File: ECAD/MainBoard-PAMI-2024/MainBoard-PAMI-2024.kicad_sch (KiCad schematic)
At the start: 41 parts, among them J1 Selecteur-Robot, J10 Serial, J2 USB_B, J3 Tirette, J4 Servo, J5 Sensor_Right, J6 Sensor_Left, J7 Conn_01x04, J8 Conn_01x04, J9 Tirette, SW1 SW_Push, SW2 SW_Push, U1 ESP32-S3-WROOM-1, U2 AMS1117-3.3, U3 Photointerrupteur

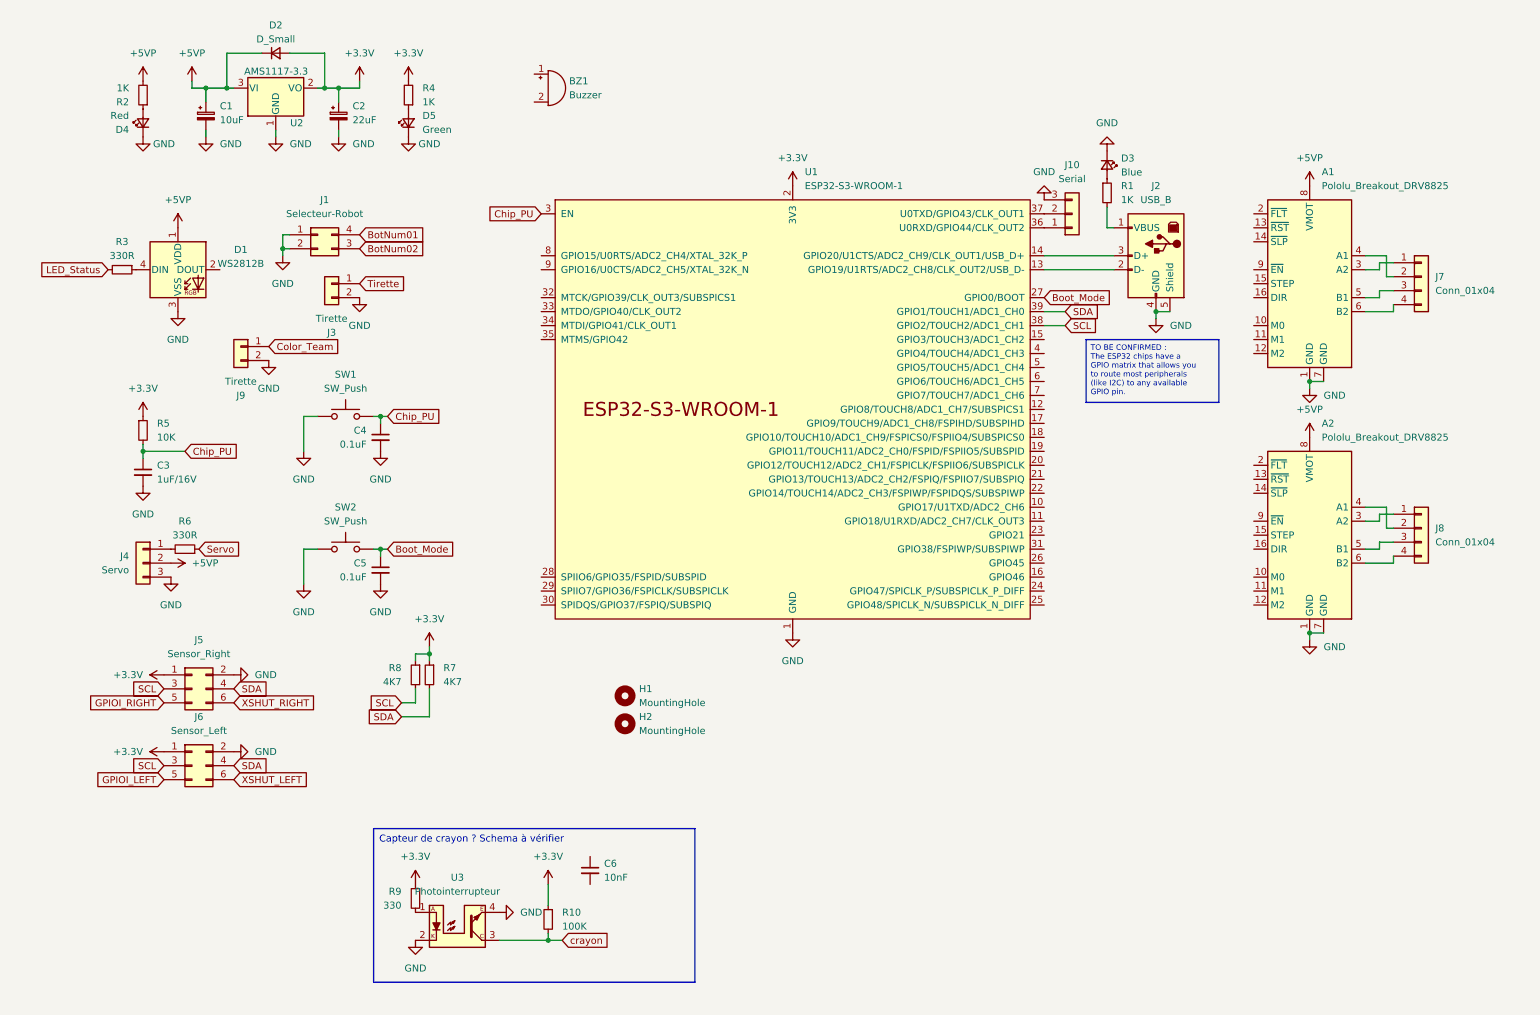
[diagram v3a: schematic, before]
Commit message: add TMC2208 reorgnise components
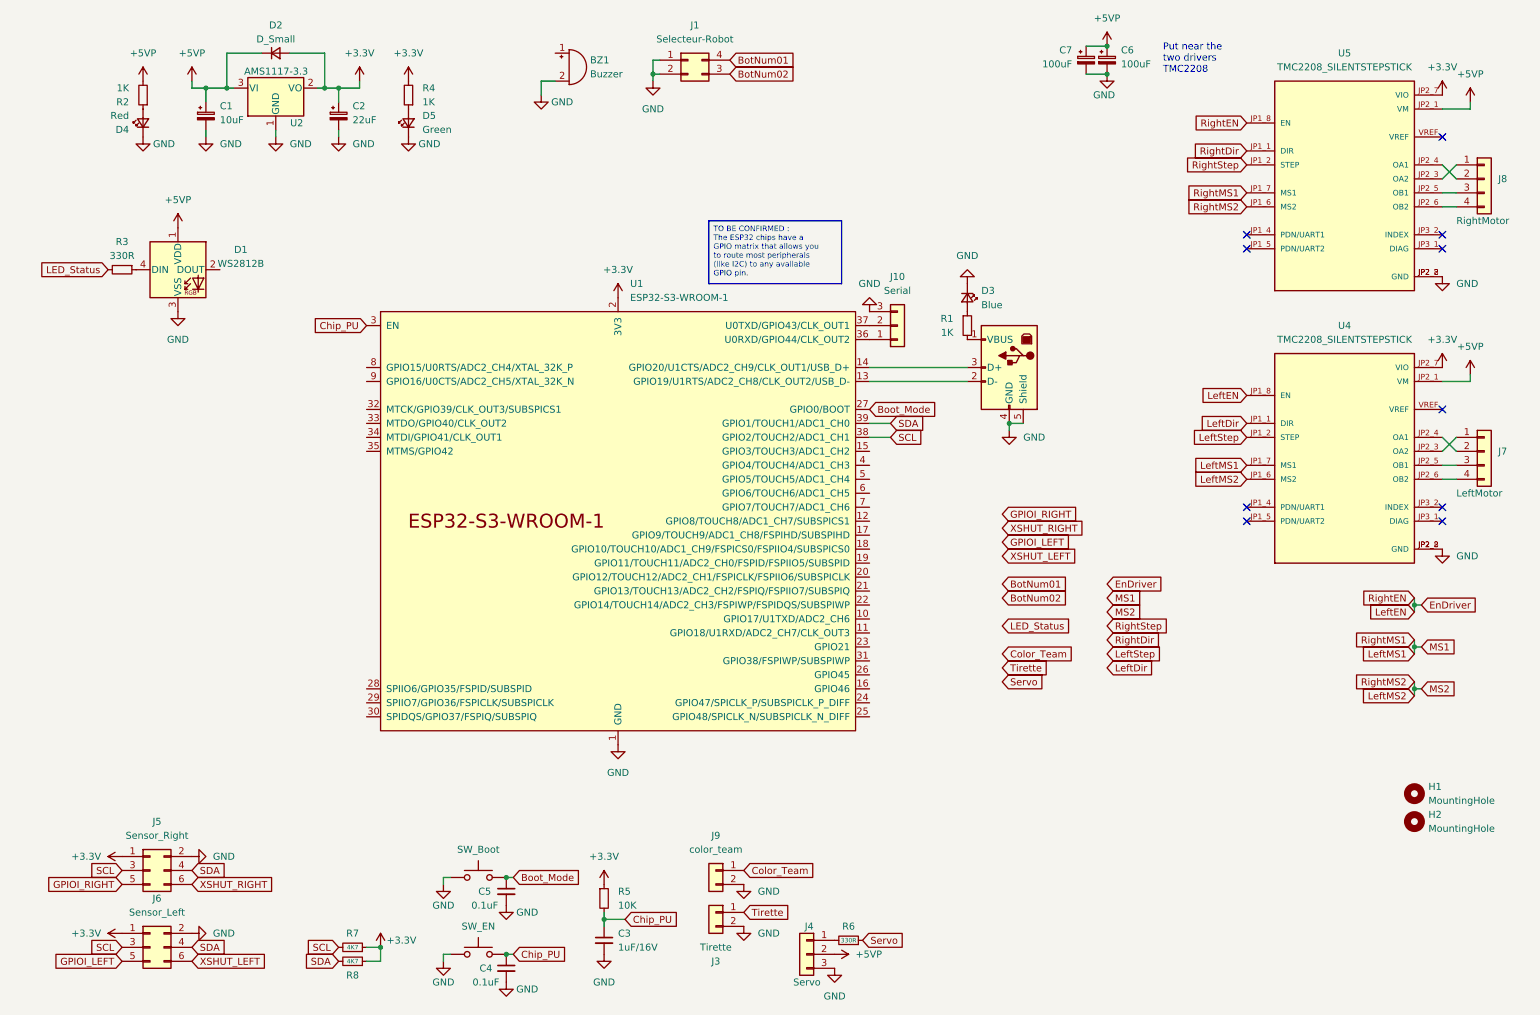
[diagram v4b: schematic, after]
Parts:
- removed A1, A2: Pololu_Breakout_DRV8825, Module:Pololu_Breakout-16_15.2x20.3mm, symbol Driver_Motor:Pololu_Breakout_DRV8825
- removed C6: 10nF, symbol Device:C_Small
- removed R10: 100K, Resistor_SMD:R_1206_3216Metric_Pad1.30x1.75mm_HandSolder, symbol Device:R_Small
- removed R9: 330, Resistor_SMD:R_1206_3216Metric_Pad1.30x1.75mm_HandSolder, symbol Device:R_Small
- removed U3: Photointerrupteur, symbol Sensor_Proximity:ITR9608-F
- added C6, C7: 100uF, symbol Device:C_Polarized_Small
- added U4, U5: TMC2208_SILENTSTEPSTICK, TMC2208_SILENTSTEPSTICK:MODULE_TMC2208_SILENTSTEPSTICK, symbol TMC2208_SILENTSTEPSTICK:TMC2208_SILENTSTEPSTICK
- BZ1: footprint (none) -> Buzzer_Beeper:Buzzer_12x9.5RM7.6
- J7: value Conn_01x04 -> LeftMotor
- J8: value Conn_01x04 -> RightMotor
- J9: value Tirette -> color_team
- SW1: value SW_Push -> SW_EN
- SW2: value SW_Push -> SW_Boot
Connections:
- net +3.3V: now also U4.JP2_7 (VIO), U5.JP2_7 (VIO)
- net +5VP: now also C6.1, C7.1, U4.JP2_1 (VM), U5.JP2_1 (VM)
- net GND: now also BZ1.2 (+), C6.2, C7.2, U4.JP2_2 (GND), U4.JP2_8 (GND), U5.JP2_2 (GND), U5.JP2_8 (GND)
- net SCL: now also R7.2; no longer R8.2
- net SDA: now also R8.2; no longer R7.2
- net at J7.1 (Pin_1): now also U4.JP2_3 (OA2)
- net at J7.2 (Pin_2): now also U4.JP2_4 (OA1)
- net at J7.3 (Pin_3): now also U4.JP2_5 (OB1)
- net at J7.4 (Pin_4): now also U4.JP2_6 (OB2)
- net at J8.1 (Pin_1): now also U5.JP2_3 (OA2)
- net at J8.2 (Pin_2): now also U5.JP2_4 (OA1)
- net at J8.3 (Pin_3): now also U5.JP2_5 (OB1)
- net at J8.4 (Pin_4): now also U5.JP2_6 (OB2)
- new net EnDriver: U4.JP1_8 (EN), U5.JP1_8 (EN)
- new net LeftDir: U4.JP1_1 (DIR)
- new net LeftMS1: U4.JP1_7 (MS1), U5.JP1_7 (MS1)
- new net LeftMS2: U4.JP1_6 (MS2), U5.JP1_6 (MS2)
- new net LeftStep: U4.JP1_2 (STEP)
- new net RightDir: U5.JP1_1 (DIR)
- new net RightStep: U5.JP1_2 (STEP)
- no-connect marks 0 -> 10
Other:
- note added: "Put near the two drivers TMC2208"
- moved on the sheet: BZ1, C3, C4, C5, D3, H1, H2, J1, J10, J3, J4, J5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

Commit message: add capacitor for ESP32
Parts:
- added C8: 0.1uF, symbol Device:C_Small
- added C9: 10uF, symbol Device:C_Small
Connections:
- net +3.3V: now also C8.1, C9.1
- net GND: now also C8.2, C9.2
- no-connect marks 10 -> 13
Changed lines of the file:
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@@
   (junction (at 68.58 29.21) (diameter 0) (color 0 0 0 0)
   )
+  (junction (at 111.76 57.15) (diameter 0) (color 0 0 0 0)
+  )
+  (junction (at 111.76 62.23) (diameter 0) (color 0 0 0 0)
+  )
   (junction (at 101.6 172.72) (diameter 0) (color 0 0 0 0)
   )
   (junction (at 193.04 90.17) (diameter 0) (color 0 0 0 0)
+  )
+  (junction (at 121.92 54.61) (diameter 0) (color 0 0 0 0)
   )
   (junction (at 210.82 26.67) (diameter 0) (color 0 0 0 0)
@@
   (no_connect (at 236.22 105.41))
   (no_connect (at 236.22 58.42))
+  (no_connect (at 76.2 140.97))
   (no_connect (at 236.22 55.88))
   (no_connect (at 271.78 105.41))
+  (no_connect (at 76.2 138.43))
   (no_connect (at 271.78 87.63))
   (no_connect (at 236.22 107.95))
   (no_connect (at 271.78 107.95))
+  (no_connect (at 76.2 143.51))
   (no_connect (at 271.78 55.88))
   (no_connect (at 271.78 58.42))
@@
     (stroke (width 0) (type default))
   )
+  (wire (pts (xy 107.95 62.23) (xy 111.76 62.23))
+    (stroke (width 0) (type default))
+  )
   (wire (pts (xy 276.86 31.75) (xy 276.86 33.02))
     (stroke (width 0) (type default))
   )
+  (wire (pts (xy 111.76 57.15) (xy 111.76 54.61))
+    (stroke (width 0) (type default))
+  )
   (wire (pts (xy 193.04 90.17) (xy 195.58 90.17))
     (stroke (width 0) (type default))
@@
     (stroke (width 0) (type default))
   )
+  (wire (pts (xy 121.92 52.07) (xy 121.92 54.61))
+    (stroke (width 0) (type default))
+  )
   (wire (pts (xy 167.64 82.55) (xy 185.42 82.55))
     (stroke (width 0) (type default))
@@
     (stroke (width 0) (type default))
   )
+  (wire (pts (xy 121.92 54.61) (xy 121.92 67.31))
+    (stroke (width 0) (type default))
+  )
   (wire (pts (xy 266.7 130.81) (xy 266.7 132.08))
     (stroke (width 0) (type default))
@@
     (stroke (width 0) (type default))
   )
+  (wire (pts (xy 111.76 54.61) (xy 121.92 54.61))
+    (stroke (width 0) (type default))
+  )
   (wire (pts (xy 59.69 36.83) (xy 59.69 38.1))
     (stroke (width 0) (type default))
@@
     (stroke (width 0) (type default))
   )
+  (wire (pts (xy 111.76 62.23) (xy 111.76 63.5))
+    (stroke (width 0) (type default))
+  )
   (wire (pts (xy 276.86 82.55) (xy 271.78 82.55))
     (stroke (width 0) (type default))
@@
   )
   (wire (pts (xy 271.78 50.8) (xy 274.32 50.8))
+    (stroke (width 0) (type default))
+  )
+  (wire (pts (xy 107.95 57.15) (xy 111.76 57.15))
     (stroke (width 0) (type default))
   )
@@
     )
   )
+  (symbol (lib_id "power:GND") (at 111.76 63.5 0) (unit 1)
+    (in_bom yes) (on_board yes) (dnp no) (fields_autoplaced)
+    (property "Reference" "#PWR042" (at 111.76 69.85 0)
+      (effects (font (size 1.27 1.27)) hide)
+    )
+    (property "Value" "GND" (at 111.76 68.58 0)
+      (effects (font (size 1.27 1.27)))
+    )
+    (property "Footprint" "" (at 111.76 63.5 0)
+      (effects (font (size 1.27 1.27)) hide)
+    )
+    (property "Datasheet" "" (at 111.76 63.5 0)
+      (effects (font (size 1.27 1.27)) hide)
+    )
+    (pin "1")
+    (instances
+      (project "MainBoard-PAMI-2024"
+        (path "/d3e1aeb6-1412-4438-ac7d-372534bf2609"
+          (reference "#PWR042") (unit 1)
+        )
+      )
+    )
+  )
   (symbol (lib_id "Device:R_Small") (at 73.66 187.96 270) (mirror x) (unit 1)
     (in_bom yes) (on_board yes) (dnp no)
@@
     )
   )
+  (symbol (lib_id "Device:C_Small") (at 107.95 59.69 0) (unit 1)
+    (in_bom yes) (on_board yes) (dnp no) (fields_autoplaced)
+    (property "Reference" "C9" (at 105.41 58.4263 0)
+      (effects (font (size 1.27 1.27)) (justify right))
+    )
+    (property "Value" "10uF" (at 105.41 60.9663 0)
+      (effects (font (size 1.27 1.27)) (justify right))
+    )
+    (property "Footprint" "" (at 107.95 59.69 0)
+      (effects (font (size 1.27 1.27)) hide)
+    )
+    (property "Datasheet" "~" (at 107.95 59.69 0)
+      (effects (font (size 1.27 1.27)) hide)
+    )
+    (pin "1")
+    (pin "2")
+    (instances
+      (project "MainBoard-PAMI-2024"
+        (path "/d3e1aeb6-1412-4438-ac7d-372534bf2609"
+          (reference "C9") (unit 1)
+        )
+      )
+    )
+  )
   (symbol (lib_id "power:+3.3V") (at 78.74 185.42 0) (unit 1)
     (in_bom yes) (on_board yes) (dnp no)
@@
     )
   )
+  (symbol (lib_id "Device:C_Small") (at 111.76 59.69 0) (unit 1)
+    (in_bom yes) (on_board yes) (dnp no) (fields_autoplaced)
+    (property "Reference" "C8" (at 114.3 58.4263 0)
+      (effects (font (size 1.27 1.27)) (justify left))
+    )
+    (property "Value" "0.1uF" (at 114.3 60.9663 0)
+      (effects (font (size 1.27 1.27)) (justify left))
+    )
+    (property "Footprint" "" (at 111.76 59.69 0)
+      (effects (font (size 1.27 1.27)) hide)
+    )
+    (property "Datasheet" "~" (at 111.76 59.69 0)
+      (effects (font (size 1.27 1.27)) hide)
+    )
+    (pin "1")
+    (pin "2")
+    (instances
+      (project "MainBoard-PAMI-2024"
+        (path "/d3e1aeb6-1412-4438-ac7d-372534bf2609"
+          (reference "C8") (unit 1)
+        )
+      )
+    )
+  )
   (symbol (lib_id "Device:LED_Small") (at 35.56 35.56 90) (unit 1)
     (in_bom yes) (on_board yes) (dnp no) (fields_autoplaced)
@@
     )
   )
-  (symbol (lib_id "power:+3.3V") (at 121.92 67.31 0) (unit 1)
-    (in_bom yes) (on_board yes) (dnp no) (fields_autoplaced)
-    (property "Reference" "#PWR04" (at 121.92 71.12 0)
-      (effects (font (size 1.27 1.27)) hide)
-    )
-    (property "Value" "+3.3V" (at 121.92 62.23 0)
-      (effects (font (size 1.27 1.27)))
-    )
-    (property "Footprint" "" (at 121.92 67.31 0)
-      (effects (font (size 1.27 1.27)) hide)
-    )
-    (property "Datasheet" "" (at 121.92 67.31 0)
-      (effects (font (size 1.27 1.27)) hide)
-    )
+  (symbol (lib_id "power:+3.3V") (at 121.92 52.07 0) (unit 1)
+    (in_bom yes) (on_board yes) (dnp no) (fields_autoplaced)
+    (property "Reference" "#PWR04" (at 121.92 55.88 0)
+      (effects (font (size 1.27 1.27)) hide)
+    )
+    (property "Value" "+3.3V" (at 121.92 46.99 0)
+      (effects (font (size 1.27 1.27)))
+    )
+    (property "Footprint" "" (at 121.92 52.07 0)
+      (effects (font (size 1.27 1.27)) hide)
+    )
+    (property "Datasheet" "" (at 121.92 52.07 0)
+      (effects (font (size 1.27 1.27)) hide)
+    )

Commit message: New version
- Wire pins
- Add PCB way
- Change Cutout
- Update 3D
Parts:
- added C10: 0.1uF, Capacitor_SMD:C_1206_3216Metric, symbol Device:C_Small
- added D6, D7: D_TVS_Bidirectional_Generic, Diode_SMD:D_SOD-523, symbol PCM_Diode_TVS_AKL:D_TVS_Bidirectional_Generic
- added D8: Red, LED_SMD:LED_1206_3216Metric, symbol Device:LED_Small
- added J11: Con_Batt, Connector_Molex:Molex_KK-254_AE-6410-02A_1x02_P2.54mm_Vertical, symbol Connector_Generic:Conn_01x02
- added J12: BAU, Connector_Molex:Molex_KK-254_AE-6410-02A_1x02_P2.54mm_Vertical, symbol Connector_Generic:Conn_01x02
- added R9: 1K, Resistor_SMD:R_1206_3216Metric_Pad1.30x1.75mm_HandSolder, symbol Device:R_Small
- C6, C7: footprint (none) -> Capacitor_THT:CP_Radial_D8.0mm_P3.80mm
- C8, C9: footprint (none) -> Capacitor_SMD:C_1206_3216Metric_Pad1.33x1.80mm_HandSolder
- J3, J9: footprint Connector_PinHeader_2.54mm:PinHeader_1x02_P2.54mm_Vertical -> Connector_Molex:Molex_KK-254_AE-6410-02A_1x02_P2.54mm_Vertical
- renumbered SW2 to SWBoot1, SW1 to SWEn1
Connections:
- net +5VP: now also C10.2, J12.2 (Pin_2)
- net BotNum01: now also U1.38 (GPIO2/TOUCH2/ADC1_CH1)
- net BotNum02: now also U1.39 (GPIO1/TOUCH1/ADC1_CH0)
- net Color_Team: now also U1.6 (GPIO6/TOUCH6/ADC1_CH5)
- net EnDriver: now also U1.25 (GPIO48/SPICLK_N/SUBSPICLK_N_DIFF)
- net GND: now also C10.1, D6.1 (K), D7.1 (K), D8.1 (K), J11.1 (Pin_1)
- net LED_Status: now also U1.5 (GPIO5/TOUCH5/ADC1_CH4)
- net LeftDir: now also U1.21 (GPIO13/TOUCH13/ADC2_CH2/FSPIQ/FSPIIO7/SUBSPIQ)
- net LeftMS1: now also U1.24 (GPIO47/SPICLK_P/SUBSPICLK_P_DIFF)
- net LeftMS2: now also U1.23 (GPIO21)
- net LeftStep: now also U1.22 (GPIO14/TOUCH14/ADC2_CH3/FSPIWP/FSPIDQS/SUBSPIWP)
- net RightDir: now also U1.18 (GPIO10/TOUCH10/ADC1_CH9/FSPICS0/FSPIIO4/SUBSPICS0)
- net RightStep: now also U1.19 (GPIO11/TOUCH11/ADC2_CH0/FSPID/FSPIIO5/SUBSPID)
- net SCL: now also U1.17 (GPIO9/TOUCH9/ADC1_CH8/FSPIHD/SUBSPIHD); no longer U1.38 (GPIO2/TOUCH2/ADC1_CH1)
- net SDA: now also U1.12 (GPIO8/TOUCH8/ADC1_CH7/SUBSPICS1); no longer U1.39 (GPIO1/TOUCH1/ADC1_CH0)
- net Servo: now also U1.20 (GPIO12/TOUCH12/ADC2_CH1/FSPICLK/FSPIIO6/SUBSPICLK)
- net Tirette: now also U1.7 (GPIO7/TOUCH7/ADC1_CH6)
- net XSHUT_LEFT: now also U1.31 (GPIO38/FSPIWP/SUBSPIWP)
- net XSHUT_RIGHT: now also U1.15 (GPIO3/TOUCH3/ADC1_CH2)
- net at J2.2 (D-), U1.13 (GPIO19/U1RTS/ADC2_CH8/CLK_OUT2/USB_D-): now also D7.2 (A)
- net at J2.3 (D+), U1.14 (GPIO20/U1CTS/ADC2_CH9/CLK_OUT1/USB_D+): now also D6.2 (A)
- net DAC1: now reaches U1.10 (GPIO17/U1TXD/ADC2_CH6)
- net DAC2: now reaches U1.11 (GPIO18/U1RXD/ADC2_CH7/CLK_OUT3)
- new net: D8.2 (A), R9.1
- new net +BATT: J11.2 (Pin_2), J12.1 (Pin_1), R9.2
- no-connect marks 13 -> 21
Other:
- note added: "45 - Strapping pin 46 - Input Only"
- moved on the sheet: C1, C2, D2, D3, D4, D5, R1, R2, R4, U2

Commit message: First routing
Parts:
- removed BZ1: Buzzer, Buzzer_Beeper:Buzzer_12x9.5RM7.6, symbol Device:Buzzer
- removed J9: color_team, Connector_Molex:Molex_KK-254_AE-6410-02A_1x02_P2.54mm_Vertical, symbol Connector_Generic:Conn_01x02
- added J13: OLED, Connector_Molex:Molex_KK-254_AE-6410-04A_1x04_P2.54mm_Vertical, symbol Connector_Generic:Conn_01x04
- added R10, R11: 10K, Resistor_SMD:R_1206_3216Metric_Pad1.30x1.75mm_HandSolder, symbol Device:R_Small
- added SW1: SW_SPDT, footprints:SK-12D10 1P2T, symbol Switch:SW_SPDT
- J11: footprint Connector_Molex:Molex_KK-254_AE-6410-02A_1x02_P2.54mm_Vertical -> Connector_AMASS:AMASS_XT30U-F_1x02_P5.0mm_Vertical
- J12: footprint Connector_Molex:Molex_KK-254_AE-6410-02A_1x02_P2.54mm_Vertical -> Connector_Molex:Molex_KK-396_A-41791-0002_1x02_P3.96mm_Vertical
- R7, R8: value 4K7 -> 10K
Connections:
- net +3.3V: now also J13.3 (Pin_3), R10.1, R11.1
- net +BATT: now also J11.1 (Pin_1); no longer J11.2 (Pin_2)
- net Color_Team: now also SW1.2 (B)
- net GND: now also J11.2 (Pin_2), J13.4 (Pin_4), SW1.1 (A); no longer J11.1 (Pin_1)
- net SCL: now also J13.2 (Pin_2), R10.2
- net SDA: now also J13.1 (Pin_1), R11.2
- net D-: now reaches D7.2 (A), J2.2 (D-), U1.13 (GPIO19/U1RTS/ADC2_CH8/CLK_OUT2/USB_D-)
- net D+: now reaches D6.2 (A), J2.3 (D+), U1.14 (GPIO20/U1CTS/ADC2_CH9/CLK_OUT1/USB_D+)
- net at J10.1 (Pin_1): now also U1.37 (U0TXD/GPIO43/CLK_OUT1); no longer U1.36 (U0RXD/GPIO44/CLK_OUT2)
- net at J10.2 (Pin_2): now also U1.36 (U0RXD/GPIO44/CLK_OUT2); no longer U1.37 (U0TXD/GPIO43/CLK_OUT1)
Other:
- moved on the sheet: J10, J11, R7, R8

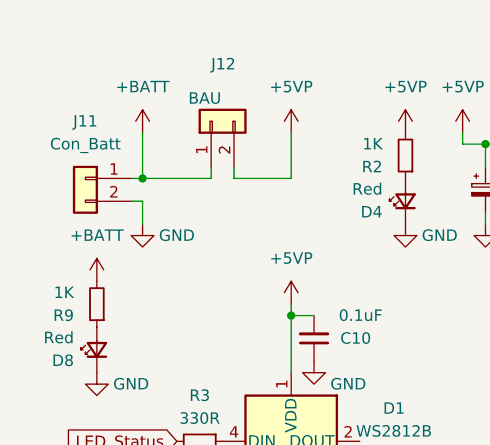
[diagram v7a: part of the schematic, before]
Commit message: Fix XT60 (Histo t'as vu)
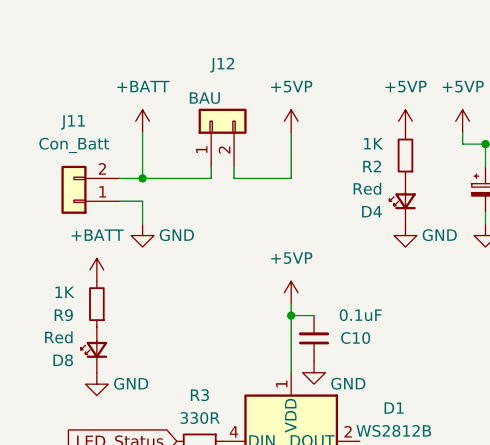
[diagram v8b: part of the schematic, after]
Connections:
- net +BATT: now also J11.2 (Pin_2); no longer J11.1 (Pin_1)
- net GND: now also J11.1 (Pin_1); no longer J11.2 (Pin_2)
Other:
- moved on the sheet: J11
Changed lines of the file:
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@@
     (stroke (width 0) (type default))
   )
-  (wire (pts (xy 24.13 33.02) (xy 25.4 33.02))
+  (wire (pts (xy 22.86 33.02) (xy 25.4 33.02))
     (stroke (width 0) (type default))
   )
@@
     (stroke (width 0) (type default))
   )
-  (wire (pts (xy 25.4 35.56) (xy 24.13 35.56))
+  (wire (pts (xy 25.4 35.56) (xy 22.86 35.56))
     (stroke (width 0) (type default))
   )
@@
     )
   )
-  (symbol (lib_id "Connector_Generic:Conn_01x02") (at 19.05 33.02 0) (mirror y) (unit 1)
+  (symbol (lib_id "Connector_Generic:Conn_01x02") (at 17.78 35.56 180) (unit 1)
     (in_bom yes) (on_board yes) (dnp no) (fields_autoplaced)
-    (property "Reference" "J11" (at 19.05 26.67 0)
+    (property "Reference" "J11" (at 17.78 26.67 0)
       (effects (font (size 1.27 1.27)))
     )
-    (property "Value" "Con_Batt" (at 19.05 29.21 0)
+    (property "Value" "Con_Batt" (at 17.78 29.21 0)
       (effects (font (size 1.27 1.27)))
     )
-    (property "Footprint" "Connector_AMASS:AMASS_XT30U-F_1x02_P5.0mm_Vertical" (at 19.05 33.02 0)
-      (effects (font (size 1.27 1.27)) hide)
-    )
-    (property "Datasheet" "~" (at 19.05 33.02 0)
-      (effects (font (size 1.27 1.27)) hide)
-    )
+    (property "Footprint" "Connector_AMASS:AMASS_XT30U-F_1x02_P5.0mm_Vertical" (at 17.78 35.56 0)
+      (effects (font (size 1.27 1.27)) hide)
+    )
+    (property "Datasheet" "~" (at 17.78 35.56 0)
+      (effects (font (size 1.27 1.27)) hide)
+    )
